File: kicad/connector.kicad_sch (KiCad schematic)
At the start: 5 parts, among them J1 Bus_M.2_Socket_E

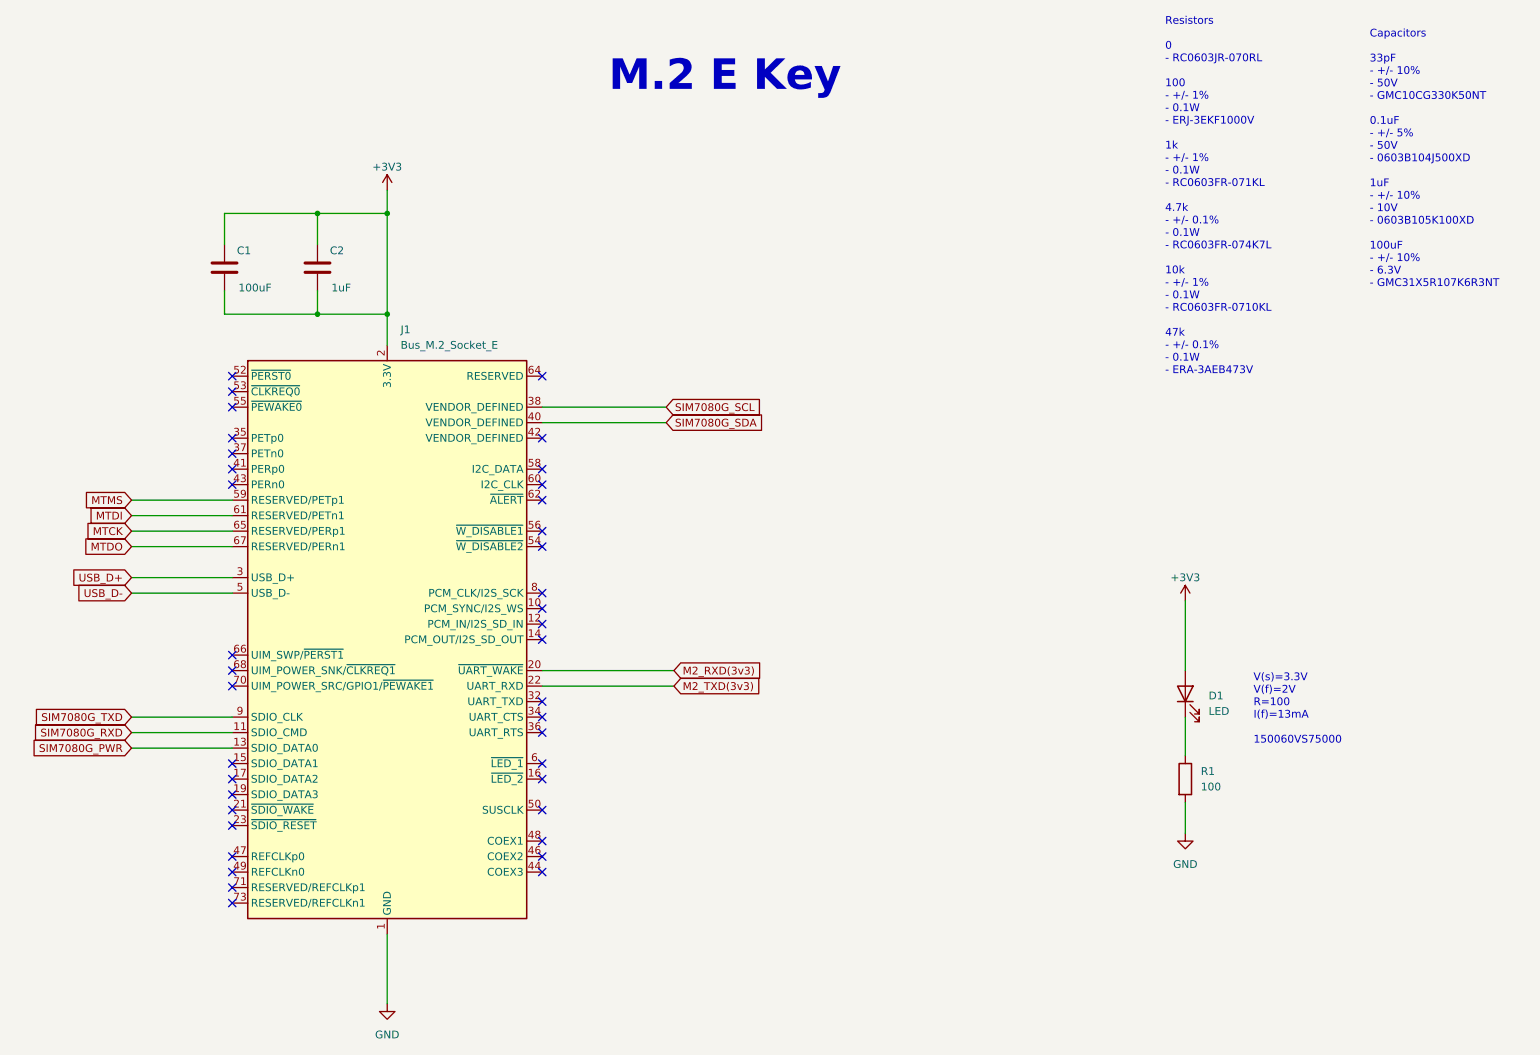
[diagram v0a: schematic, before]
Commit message: Update level shifter schematic
Signed-off-by: JeffMboya <jangina.mboya@gmail.com>
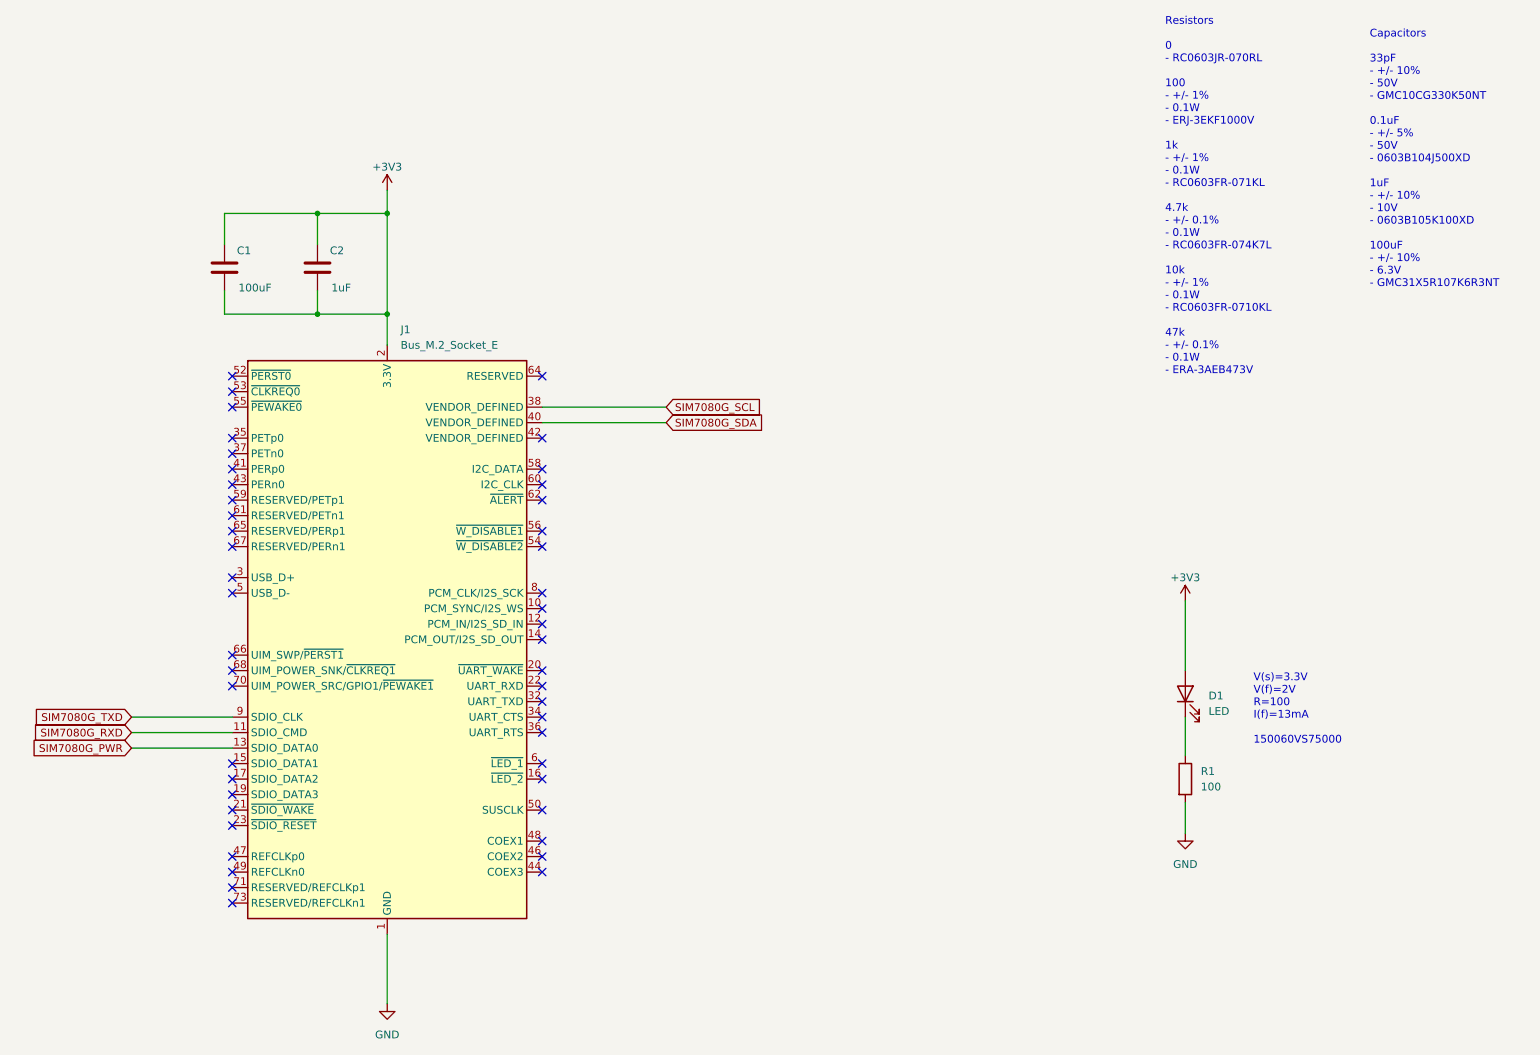
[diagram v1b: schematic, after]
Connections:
- net M2_RXD(3v3): no longer names the net of J1.20 (~{UART_WAKE})
- net M2_TXD(3v3): no longer names the net of J1.22 (UART_RXD)
- net MTCK: no longer names the net of J1.65 (RESERVED/PERp1)
- net MTDI: no longer names the net of J1.61 (RESERVED/PETn1)
- net MTDO: no longer names the net of J1.67 (RESERVED/PERn1)
- net MTMS: no longer names the net of J1.59 (RESERVED/PETp1)
- net USB_D+: no longer names the net of J1.3 (USB_D+)
- net USB_D-: no longer names the net of J1.5 (USB_D-)
- no-connect marks 39 -> 47
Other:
- note removed: "M.2 E Key"

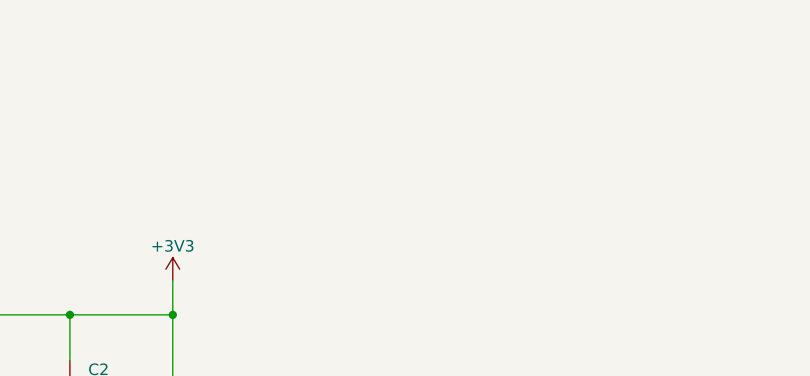
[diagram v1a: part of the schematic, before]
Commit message: Remove unnecessary pages
Signed-off-by: JeffMboya <jangina.mboya@gmail.com>
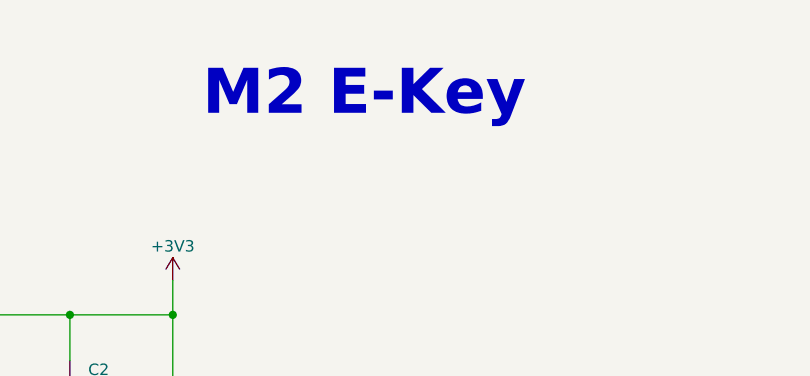
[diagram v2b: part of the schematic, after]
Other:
- note added: "M2 E-Key"
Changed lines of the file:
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@@
+		)
+	)
+	(text "M2 E-Key"
+		(exclude_from_sim no)
+		(at 98.552 26.67 0)
+		(effects
+			(font
+				(size 5 5)
+				(thickness 1)
+				(bold yes)
+			)
+			(justify left bottom)
 		)
 	)
